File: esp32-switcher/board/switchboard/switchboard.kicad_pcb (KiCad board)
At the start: 2 copper layers, 68.5 x 46 mm, 15 parts, among them J1 Conn_01x03, J10 Conn_01x02, J11 Conn_01x02, J12 Conn_01x02, J13 Conn_01x02, J14 Conn_01x02, J2 Conn_01x04, J3 Conn_01x02, J4 Conn_01x02, J5 Conn_01x02, J6 Conn_01x02, J7 Conn_01x02, J8 Conn_01x02, J9 Conn_01x02, U1 ESP32-DEVKITC-32D

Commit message: Updates, almost ready to go
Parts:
- removed the J1 at (160.3, 128.3)
- removed the J2 at (158.8, 114.8)
- added J15: Chain Out, Connector_JST:JST_XH_B3B-XH-AM_1x03_P2.50mm_Vertical, B.Cu at (136.1, 115.4)
- added J16: Chain In, Connector_JST:JST_XH_B3B-XH-AM_1x03_P2.50mm_Vertical, B.Cu at (126.3, 115.4)
- added J17: Conn_01x04, Connector_PinSocket_2.54mm:PinSocket_1x04_P2.54mm_Vertical, F.Cu at (152.0, 111.7)
- added REF**: OSHW-Logo2_9.8x8mm_SilkScreen, Symbol:OSHW-Logo2_9.8x8mm_SilkScreen, B.Cu at (145.2, 112.8)
- added REF**: KiCad-Logo2_8mm_SilkScreen, Symbol:KiCad-Logo2_8mm_SilkScreen, B.Cu at (108.1, 112.8)
- U1: value ESP32-DEVKITC-32D -> NODEMCU-32S
- renumbered J3 to J1, J9 to J11, J8 to J12, J4 to J2, J5 to J3, J6 to J4, J7 to J5, J14 to J6, J13 to J7, J12 to J8, J11 to J9
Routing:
- net Net-(J15-Pad3): track 46.1 -> 30.7 mm
- net Net-(J15-Pad1): track 38.1 -> 24.8 mm
- net PWR: track 14.8 -> 7.64 mm
- net Net-(J17-Pad2): track 46.7 -> 40.6 mm
- net Net-(J17-Pad3): track 50.9 -> 46.6 mm
- net Net-(J6-Pad1): track 54.2 -> 53.0 mm
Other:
- board size 68.5 x 46 mm -> 59.5 x 48 mm
- board text added: "https://github.com/rattboi/extron-scart-adapter/"
- board text added: "v1"

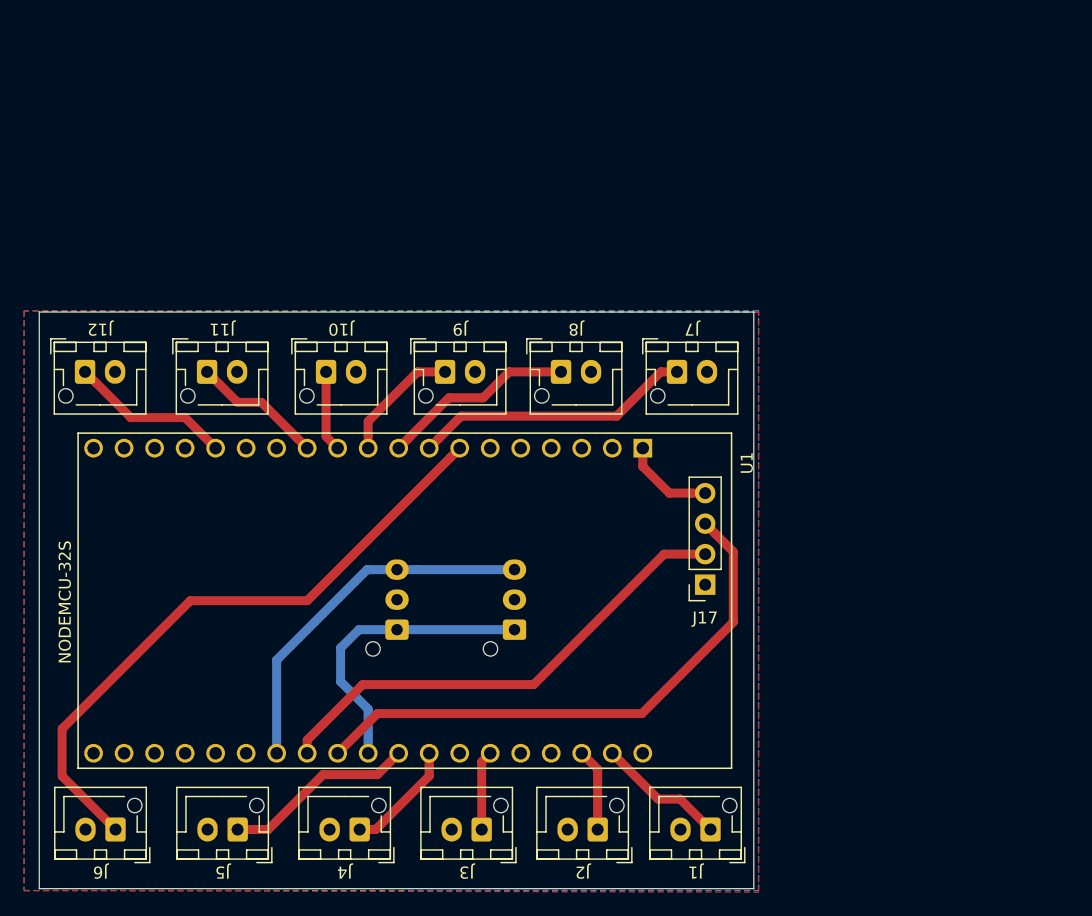
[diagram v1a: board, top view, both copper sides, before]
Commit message: Rev 1.1 of ESP32 Switchboard
I think this rev is basically ready to go. I could see someone using
this for real. I still have a lot of software features I wanna add, but
the hardware is basically complete.

I may come back and add a built-in serial port, as the little breakout
can be flimsy, but it seems that 3v3 rs232 stuff means SMD components,
and I've been trying to avoid that to make this easier to DIY.

board:
  Converted footprint to Kicad non-legacy
  Fixed footprint to be HiLetGo ESP-E32, which is narrower than NodeMCU
  Fixed up references on schematic to be in order
  Flipped mistaken footprint on RS232 UART breakout

code:
  Added support for all 12 inputs
  IRQ-based on rising/falling edges
  Added 0.1s timer-based timeout for input switch after input off
    Fixes some bouncing in the signal I didn't expect when powering off
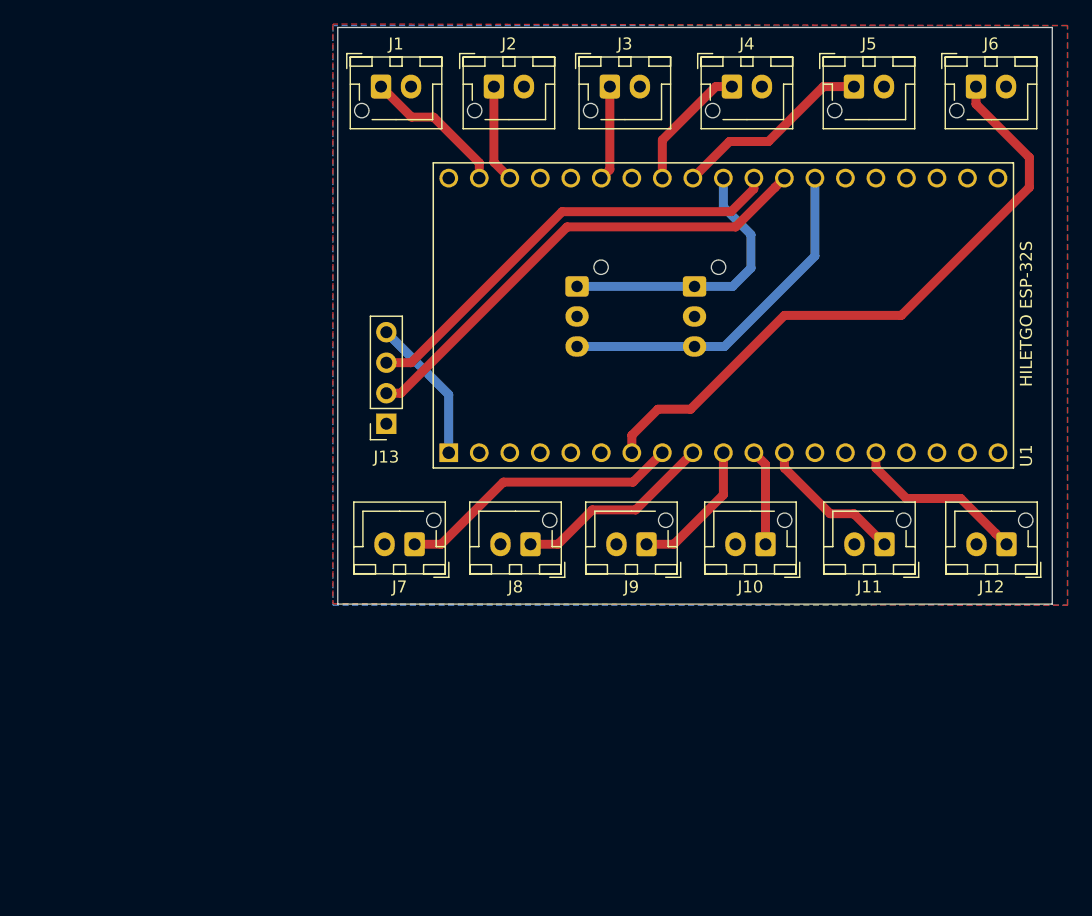
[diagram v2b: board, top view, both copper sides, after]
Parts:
- removed J17: Conn_01x04, Connector_PinSocket_2.54mm:PinSocket_1x04_P2.54mm_Vertical
- added J13: Conn_01x04, Connector_PinSocket_2.54mm:PinSocket_1x04_P2.54mm_Vertical, F.Cu at (125.4, 98.3)
- U1: value NODEMCU-32S -> HILETGO ESP-32S; footprint ESP32-DEVKITC-32D:MODULE_ESP32-DEVKITC-32D -> hiletgo-e32:HILETGO-E32
- moved J6 94.6 mm to (174.5, 70.2), turned to 0 degrees
- moved J5 80.4 mm to (164.3, 70.2), turned to 0 degrees
- moved J12 78.0 mm to (177.0, 108.3), turned to 180 degrees
- moved J4 69.2 mm to (154.2, 70.2), turned to 0 degrees
- moved J1 67.7 mm to (125.0, 70.2), turned to 0 degrees
- moved REF** 65.5 mm to (169.3, 89.5), turned to 180 degrees
- moved J3 62.8 mm to (144.0, 70.2), turned to 0 degrees
- moved J2 62.4 mm to (134.4, 70.2), turned to 0 degrees
- moved J11 58.2 mm to (166.9, 108.3), turned to 180 degrees
- moved J10 39.3 mm to (157.0, 108.3), turned to 180 degrees
- moved J15 37.8 mm to (151.1, 86.9), turned to 270 degrees
- moved U1 33.3 mm to (150.4, 89.3), turned to 90 degrees
- moved J14 29.0 mm to (141.3, 86.9), turned to 270 degrees
- moved REF** 26.7 mm to (132.2, 89.5), turned to 180 degrees
- moved J7 26.1 mm to (127.8, 108.3), turned to 180 degrees
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- renumbered J15 to J14, J16 to J15
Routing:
- net Net-(J13-Pad3): track 46.6 -> 37.5 mm
- net PWR: track 7.64 -> 12.2 mm
- net Net-(J9-Pad1): track 10.3 -> 11.6 mm
- net Net-(J12-Pad1): track 13.5 -> 14.8 mm
- net Net-(J10-Pad1): track 6.75 -> 8.02 mm
- net Net-(J14-Pad3): track 30.7 -> 29.4 mm
- net Net-(J4-Pad1): track 9.53 -> 10.8 mm
- net Net-(J3-Pad1): track 6.64 -> 7.91 mm
- net Net-(J14-Pad1): track 24.8 -> 23.6 mm
- net Net-(J11-Pad1): track 11.0 -> 12.2 mm
- net Net-(J1-Pad1): track 10.8 -> 12.1 mm
- net Net-(J2-Pad1): track 6.90 -> 8.17 mm
- net Net-(J8-Pad1): track 16.1 -> 16.7 mm
- net Net-(J7-Pad1): track 23.3 -> 23.8 mm
- net Net-(J5-Pad1): track 16.0 -> 16.6 mm
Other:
- board text added: "v1.1"
- board text removed: "v1"
